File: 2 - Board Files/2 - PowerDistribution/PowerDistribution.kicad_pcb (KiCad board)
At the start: 6 copper layers, 100.1 x 100.1 mm, 41 parts, among them J201 Battery Input, J202 Battery Balance Connector, U201 MAX40056F, U202 MAX40056F

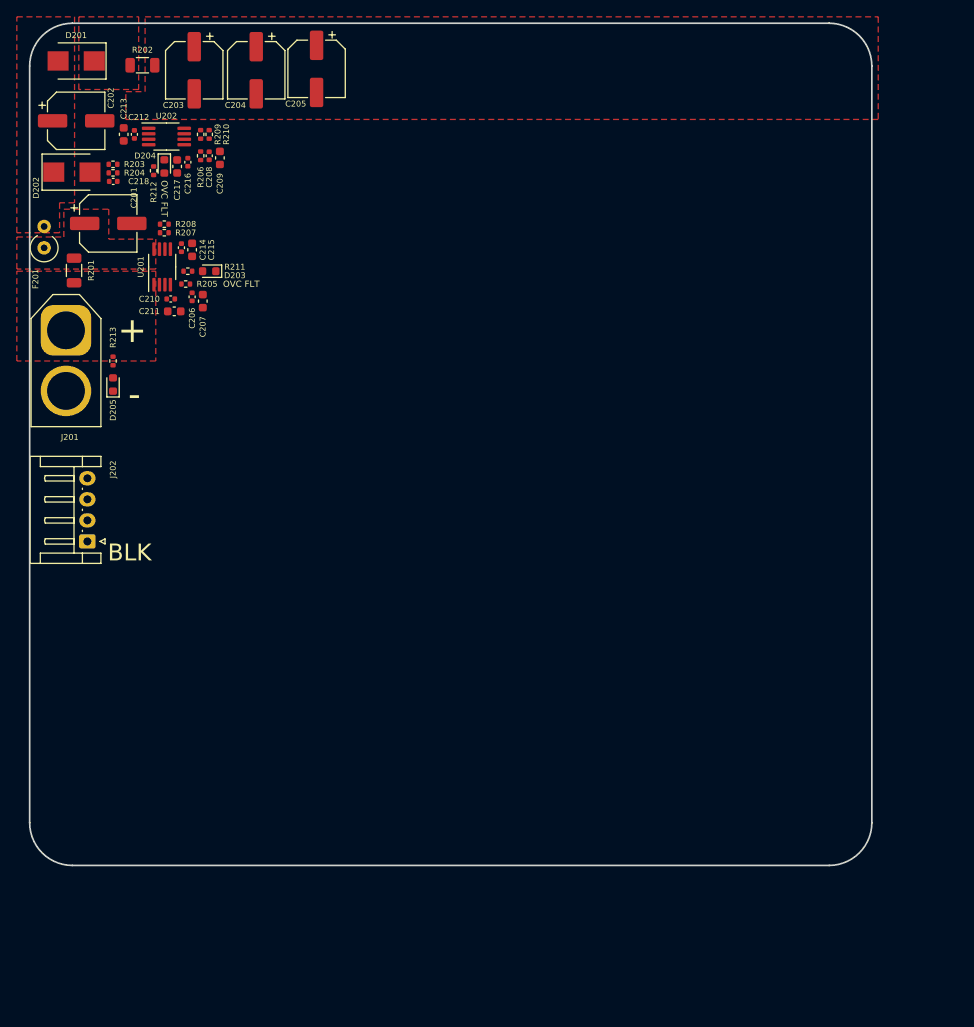
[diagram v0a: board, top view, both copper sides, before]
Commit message: Part values for power input stage
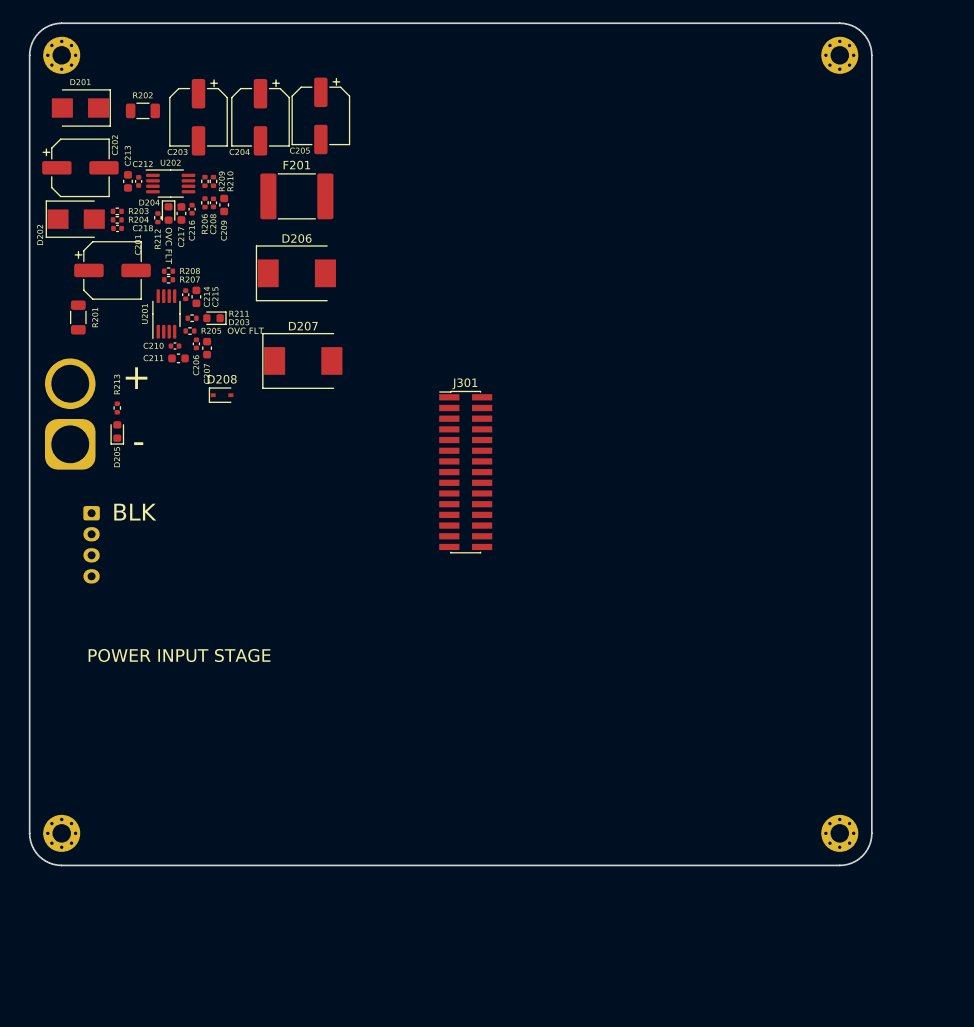
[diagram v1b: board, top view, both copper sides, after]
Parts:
- added D206: D_TVS, Diode_SMD:D_SMC, F.Cu at (127.3, 71.4)
- added D207: D_TVS, Diode_SMD:D_SMC, F.Cu at (128.0, 81.8)
- added D208: D_Zener, Diode_SMD:D_SOD-323, F.Cu at (118.4, 85.9)
- added H101: MountingHole, MountingHole:MountingHole_2.2mm_M2_Pad_Via, F.Cu at (191.8, 45.5)
- added H102: MountingHole, MountingHole:MountingHole_2.2mm_M2_Pad_Via, F.Cu at (99.3, 137.9)
- added H103: MountingHole, MountingHole:MountingHole_2.2mm_M2_Pad_Via, F.Cu at (191.8, 137.9)
- added H104: MountingHole, MountingHole:MountingHole_2.2mm_M2_Pad_Via, F.Cu at (99.3, 45.5)
- added J301: Conn_02x15_Counter_Clockwise, Connector_PinHeader_1.27mm:PinHeader_2x15_P1.27mm_Vertical_SMD, F.Cu at (147.3, 95.0)
- F201: footprint Resistor_THT:R_Axial_DIN0309_L9.0mm_D3.2mm_P2.54mm_Vertical -> Fuse:Fuse_2920_7451Metric
- J201, J202: moved to B.Cu
- R201: value BATT_SNS_SHUNT -> 1m, 3W
- R202: value CTL_PWR_SHUNT -> 22m, 3W
- R203: value R_Small_US -> 22k
- R204: value R_Small_US -> 82k
- R205, R206: value R_Small_US -> 150R
- R207: value R_Small_US -> 6k8
- R208: value R_Small_US -> 3k3
- R209, R211, R212: value R_Small_US -> 1k2
- R210: value R_Small_US -> 9k1
- moved F201 30.6 mm to (127.3, 62.2), turned to 0 degrees
- moved J201 13.6 mm to (100.3, 91.7), turned to 90 degrees
- moved C214 5.61 mm to (114.0, 73.9)
- moved D205 5.61 mm to (105.9, 90.2)
- moved R213 5.61 mm to (105.9, 87.4)
- moved U201 5.61 mm to (111.8, 76.2)
- moved C210 5.61 mm to (112.8, 80.0)
- moved C211 5.61 mm to (113.2, 81.5)
- moved C215 5.61 mm to (115.3, 74.2)
- moved C218 5.61 mm to (105.9, 66.0)
- moved D202 5.61 mm to (101.0, 64.9)
- moved R201 5.61 mm to (101.3, 76.6)
- moved R208 5.61 mm to (112.0, 71.1)
- moved C202 5.61 mm to (101.5, 58.8)
- moved C204 5.61 mm to (122.9, 52.8)
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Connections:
- net BATT_CELL1 renamed /BatteryInput/BATT_CELL1
- net BATT_CELL2 renamed /BatteryInput/BATT_CELL2
- net BATT_CELL3 renamed /BatteryInput/BATT_CELL3
- net BATT_CURR_MON renamed /BATT_I_MON
- net BATT_V_SNS renamed /BATT_V_MON
- net Net-(C214-Pad1) renamed /BatteryInput/BATT_SNS_REF
- net Net-(C216-Pad1) renamed /BatteryInput/VDC_SNS_REF
- net Net-(R205-Pad1) renamed /BatteryInput/BATT_SNS_OUT
- net Net-(R206-Pad1) renamed /BatteryInput/VDC_SNS_OUT
- net Net-(R207-Pad2) renamed /BatteryInput/BATT_SNS_CIP
- net Net-(R209-Pad2) renamed /BatteryInput/VDC_SNS_CIP
- net VDC_CURR_MON renamed /VDC_I_MON
- C201 pad 1: /BatteryInput/BAT+_IN_SNS -> +BATT
- D201 pad 2: +BATT -> Net-(D201-Pad2)
- D202 pad 1: +BATT -> Net-(D201-Pad2)
- F201 pad 1: /BatteryInput/BAT+_IN_SNS -> +BATT
- F201 pad 2: +BATT -> Net-(D201-Pad2)
- J201 pad 1: /BatteryInput/BAT+_IN -> GND
- J201 pad 2: GND -> /BatteryInput/BAT+_IN
- R201 pad 2: /BatteryInput/BAT+_IN_SNS -> +BATT
- R203 pad 2: +BATT -> Net-(D201-Pad2)
- U201 pad 1: /BatteryInput/BAT+_IN -> +BATT
- U201 pad 8: /BatteryInput/BAT+_IN_SNS -> /BatteryInput/BAT+_IN
- U202 pad 1: /BatteryInput/VDC_SNS_IN -> VDC
- U202 pad 8: VDC -> /BatteryInput/VDC_SNS_IN
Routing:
- removed copper zone on F.Cu, net +BATT
- removed copper zone on F.Cu, net /BatteryInput/BAT+_IN
- removed copper zone on F.Cu, net /BatteryInput/BAT+_IN_SNS
- removed copper zone on F.Cu, net /BatteryInput/VDC_SNS_IN
- removed copper zone on F.Cu, net VDC
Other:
- outline, holes or cut-outs redrawn
- board text added: "POWER INPUT STAGE"

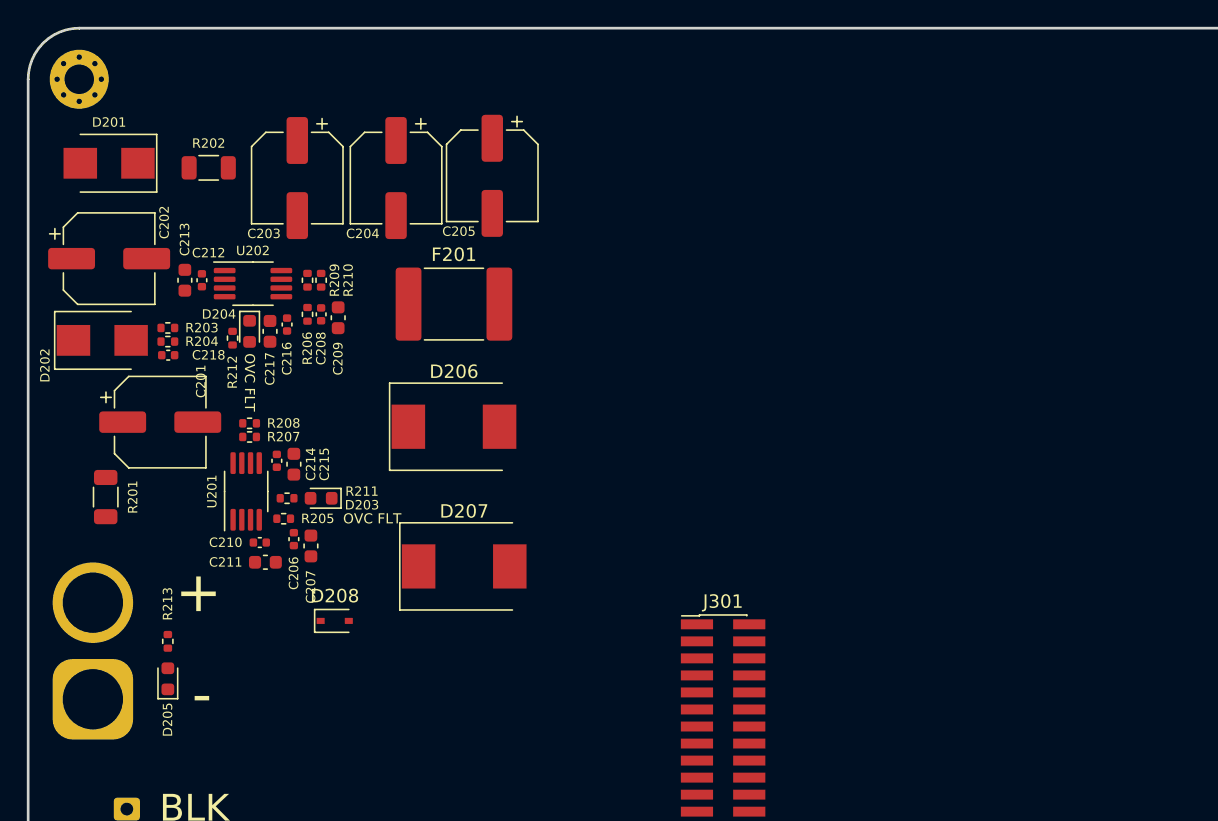
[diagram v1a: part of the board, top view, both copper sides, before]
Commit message: Added switching regulator
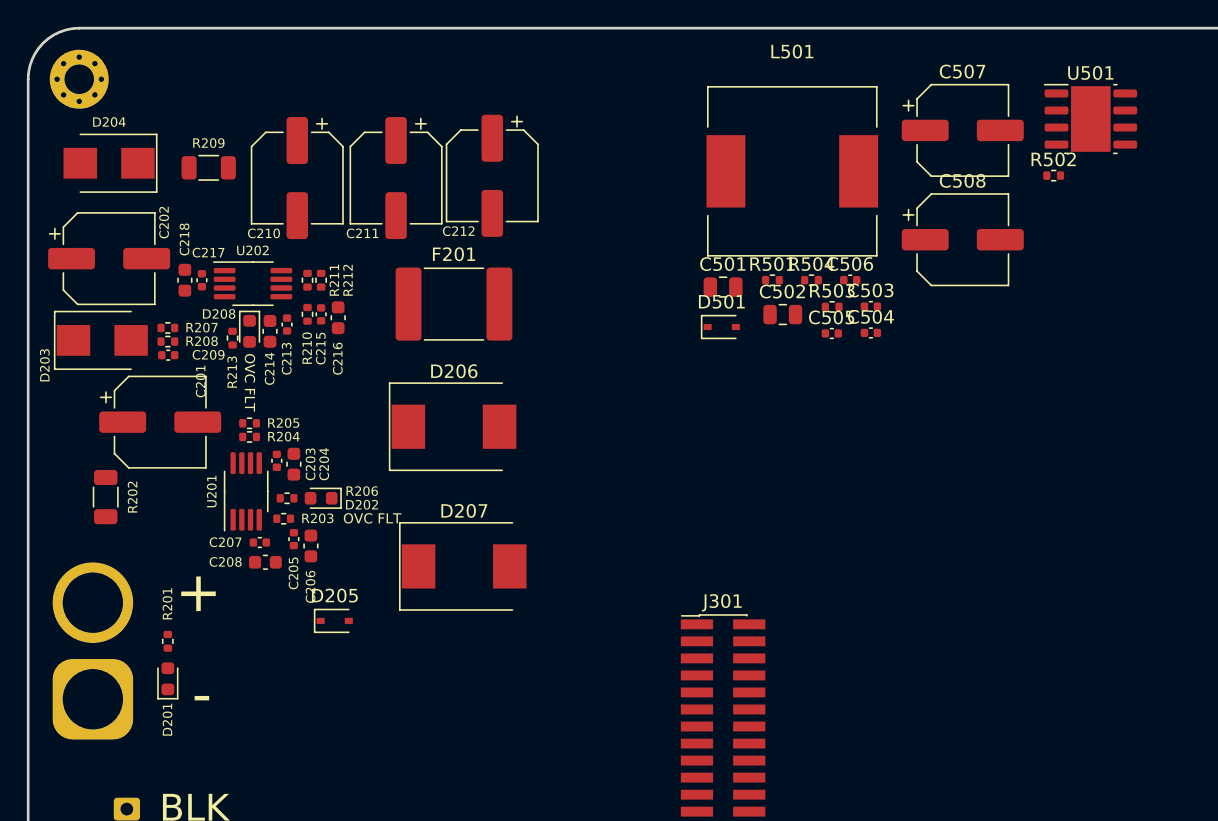
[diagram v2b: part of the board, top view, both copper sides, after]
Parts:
- added C501: 1u, Capacitor_SMD:C_0805_2012Metric, F.Cu at (147.3, 61.0)
- added C502: 4u2, Capacitor_SMD:C_0805_2012Metric, F.Cu at (151.8, 63.0)
- added C503: 0u1, Capacitor_SMD:C_0402_1005Metric, F.Cu at (158.3, 62.4)
- added C504: C_Small, Capacitor_SMD:C_0402_1005Metric, F.Cu at (158.3, 64.4)
- added C505: 10n, Capacitor_SMD:C_0402_1005Metric, F.Cu at (155.4, 64.4)
- added C506: C_Small, Capacitor_SMD:C_0402_1005Metric, F.Cu at (156.8, 60.4)
- added C507: 10u, Capacitor_SMD:CP_Elec_6.3x5.4, F.Cu at (165.2, 49.3)
- added C508: 10u, Capacitor_SMD:CP_Elec_6.3x5.4, F.Cu at (165.2, 57.4)
- added D501: D_Zener, Diode_SMD:D_SOD-323, F.Cu at (147.2, 63.9)
- added L501: 3u3, Inductor_SMD:L_12x12mm_H4.5mm, F.Cu at (152.5, 52.3)
- added R501: R_Small_US, Resistor_SMD:R_0402_1005Metric, F.Cu at (151.0, 60.5)
- added R502: R_Small_US, Resistor_SMD:R_0402_1005Metric, F.Cu at (172.0, 52.6)
- added R503: 68k1, Resistor_SMD:R_0402_1005Metric, F.Cu at (155.4, 62.4)
- added R504: 15k, Resistor_SMD:R_0402_1005Metric, F.Cu at (153.9, 60.5)
- added U501: AOZ6605PI, Package_SO:SOIC-8-1EP_3.9x4.9mm_P1.27mm_EP2.95x4.9mm_Mask2.71x3.4mm, F.Cu at (174.7, 48.4)
- renumbered C214 to C203, C215 to C204, C206 to C205, C207 to C206, C210 to C207, C211 to C208, C218 to C209, C203 to C210, C204 to C211, C205 to C212, C216 to C213, C217 to C214, C208 to C215, C209 to C216, C212 to C217, C213 to C218, D205 to D201, D203 to D202, D202 to D203, D201 to D204, D208 to D205, D204 to D208, H103 to H102, H102 to H103, R213 to R201, R201 to R202, R205 to R203, R207 to R204, R208 to R205, R211 to R206, R203 to R207, R204 to R208, R202 to R209, R206 to R210, R209 to R211, R210 to R212, R212 to R213
